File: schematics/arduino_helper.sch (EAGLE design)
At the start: 8 parts, among them Q1 L78M05CDT

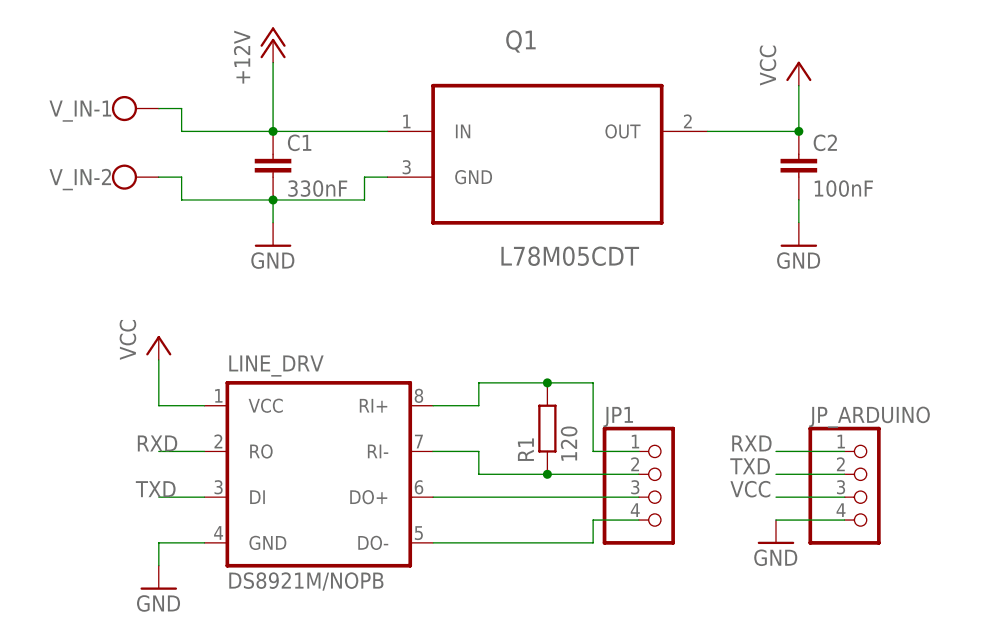
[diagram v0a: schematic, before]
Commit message: Extra caps, wider supply traces for the Arduino helper PCB.
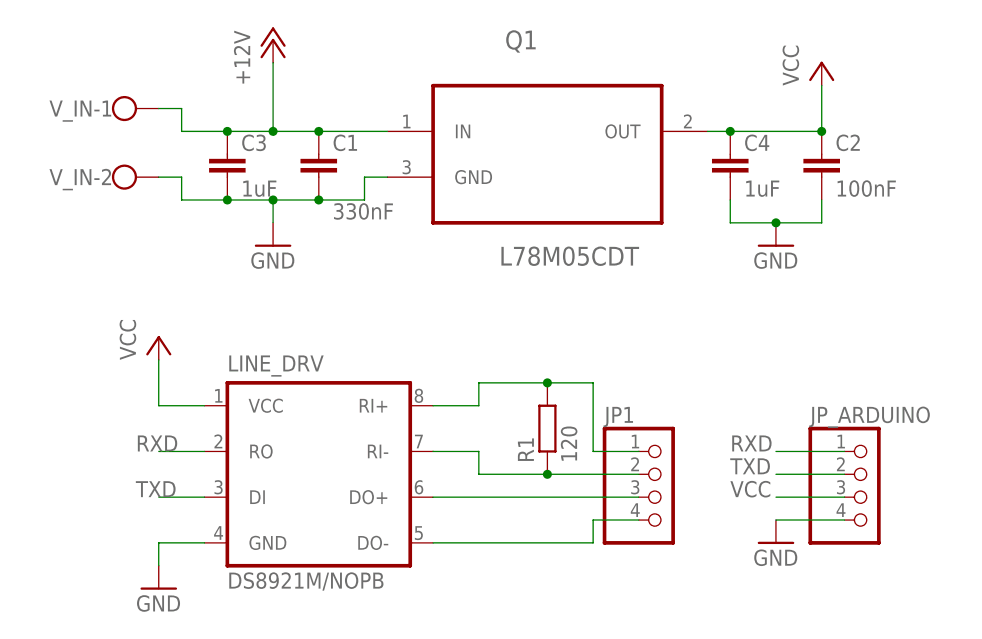
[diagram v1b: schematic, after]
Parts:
- added C3, C4: 1uF, rcl:C-EUC0805
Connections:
- net +12V: now also C3.1
- net GND: now also C3.2, C4.2
- net VCC: now also C4.1
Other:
- moved on the sheet: C1, C2
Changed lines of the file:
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@@
 <part name="GND4" library="supply1" deviceset="GND" device=""/>
 <part name="P+3" library="supply1" deviceset="+12V" device=""/>
+<part name="C3" library="rcl" deviceset="C-EU" device="C0805" value="1uF"/>
+<part name="C4" library="rcl" deviceset="C-EU" device="C0805" value="1uF"/>
 </parts>
 <sheets>
@@
 <instance part="V_IN" gate="-2" x="7.62" y="25.4"/>
 <instance part="JP1" gate="A" x="68.58" y="-10.16"/>
-<instance part="C1" gate="G$1" x="25.4" y="27.94"/>
-<instance part="C2" gate="G$1" x="83.82" y="27.94"/>
-<instance part="GND1" gate="1" x="83.82" y="17.78"/>
-<instance part="P+1" gate="VCC" x="83.82" y="38.1"/>
+<instance part="C1" gate="G$1" x="30.48" y="27.94" smashed="yes">
+<attribute name="NAME" x="32.004" y="28.321" size="1.778" layer="95"/>
+<attribute name="VALUE" x="32.004" y="20.701" size="1.778" layer="96"/>
+</instance>
+<instance part="C2" gate="G$1" x="86.36" y="27.94"/>
+<instance part="GND1" gate="1" x="81.28" y="17.78"/>
+<instance part="P+1" gate="VCC" x="86.36" y="38.1"/>
 <instance part="GND2" gate="1" x="25.4" y="17.78"/>
 <instance part="P+2" gate="VCC" x="12.7" y="7.62"/>
@@
 <instance part="GND4" gate="1" x="81.28" y="-15.24"/>
 <instance part="P+3" gate="1" x="25.4" y="40.64"/>
+<instance part="C3" gate="G$1" x="20.32" y="27.94"/>
+<instance part="C4" gate="G$1" x="76.2" y="27.94"/>
 </instances>
 <busses>
@@
 <segment>
 <pinref part="C2" gate="G$1" pin="2"/>
-<wire x1="83.82" y1="22.86" x2="83.82" y2="20.32" width="0.1524" layer="91"/>
 <pinref part="GND1" gate="1" pin="GND"/>
+<pinref part="C4" gate="G$1" pin="2"/>
+<wire x1="76.2" y1="22.86" x2="76.2" y2="20.32" width="0.1524" layer="91"/>
+<wire x1="76.2" y1="20.32" x2="81.28" y2="20.32" width="0.1524" layer="91"/>
+<wire x1="81.28" y1="20.32" x2="86.36" y2="20.32" width="0.1524" layer="91"/>
+<wire x1="86.36" y1="20.32" x2="86.36" y2="22.86" width="0.1524" layer="91"/>
+<junction x="81.28" y="20.32"/>
 </segment>
 <segment>
@@
 <wire x1="35.56" y1="25.4" x2="35.56" y2="22.86" width="0.1524" layer="91"/>
 <pinref part="C1" gate="G$1" pin="2"/>
-<wire x1="35.56" y1="22.86" x2="25.4" y2="22.86" width="0.1524" layer="91"/>
-<wire x1="25.4" y1="22.86" x2="15.24" y2="22.86" width="0.1524" layer="91"/>
+<wire x1="35.56" y1="22.86" x2="30.48" y2="22.86" width="0.1524" layer="91"/>
+<wire x1="30.48" y1="22.86" x2="25.4" y2="22.86" width="0.1524" layer="91"/>
+<wire x1="25.4" y1="22.86" x2="20.32" y2="22.86" width="0.1524" layer="91"/>
+<wire x1="20.32" y1="22.86" x2="15.24" y2="22.86" width="0.1524" layer="91"/>
 <wire x1="15.24" y1="22.86" x2="15.24" y2="25.4" width="0.1524" layer="91"/>
 <pinref part="V_IN" gate="-2" pin="KL"/>
 <wire x1="15.24" y1="25.4" x2="12.7" y2="25.4" width="0.1524" layer="91"/>
+<junction x="30.48" y="22.86"/>
+<pinref part="GND2" gate="1" pin="GND"/>
+<pinref part="C3" gate="G$1" pin="2"/>
+<junction x="20.32" y="22.86"/>
+<wire x1="25.4" y1="20.32" x2="25.4" y2="22.86" width="0.1524" layer="91"/>
 <junction x="25.4" y="22.86"/>
-<wire x1="25.4" y1="22.86" x2="25.4" y2="20.32" width="0.1524" layer="91"/>
-<pinref part="GND2" gate="1" pin="GND"/>
 </segment>
 <segment>
@@
 <pinref part="Q1" gate="A" pin="OUT"/>
 <pinref part="C2" gate="G$1" pin="1"/>
-<wire x1="73.66" y1="30.48" x2="83.82" y2="30.48" width="0.1524" layer="91"/>
-<wire x1="83.82" y1="30.48" x2="83.82" y2="35.56" width="0.1524" layer="91"/>
-<junction x="83.82" y="30.48"/>
+<wire x1="73.66" y1="30.48" x2="76.2" y2="30.48" width="0.1524" layer="91"/>
+<wire x1="76.2" y1="30.48" x2="86.36" y2="30.48" width="0.1524" layer="91"/>
+<wire x1="86.36" y1="30.48" x2="86.36" y2="35.56" width="0.1524" layer="91"/>
+<junction x="86.36" y="30.48"/>
 <pinref part="P+1" gate="VCC" pin="VCC"/>
+<pinref part="C4" gate="G$1" pin="1"/>
+<junction x="76.2" y="30.48"/>
 </segment>
 <segment>
@@
 <pinref part="Q1" gate="A" pin="IN"/>
 <pinref part="C1" gate="G$1" pin="1"/>
-<wire x1="38.1" y1="30.48" x2="25.4" y2="30.48" width="0.1524" layer="91"/>
-<wire x1="25.4" y1="30.48" x2="15.24" y2="30.48" width="0.1524" layer="91"/>
+<wire x1="38.1" y1="30.48" x2="30.48" y2="30.48" width="0.1524" layer="91"/>
+<wire x1="30.48" y1="30.48" x2="25.4" y2="30.48" width="0.1524" layer="91"/>
+<wire x1="25.4" y1="30.48" x2="20.32" y2="30.48" width="0.1524" layer="91"/>
+<wire x1="20.32" y1="30.48" x2="15.24" y2="30.48" width="0.1524" layer="91"/>
 <wire x1="15.24" y1="30.48" x2="15.24" y2="33.02" width="0.1524" layer="91"/>
 <pinref part="V_IN" gate="-1" pin="KL"/>
 <wire x1="15.24" y1="33.02" x2="12.7" y2="33.02" width="0.1524" layer="91"/>
+<junction x="30.48" y="30.48"/>
+<pinref part="P+3" gate="1" pin="+12V"/>
+<pinref part="C3" gate="G$1" pin="1"/>
+<junction x="20.32" y="30.48"/>
+<wire x1="25.4" y1="38.1" x2="25.4" y2="30.48" width="0.1524" layer="91"/>
 <junction x="25.4" y="30.48"/>
-<wire x1="25.4" y1="30.48" x2="25.4" y2="38.1" width="0.1524" layer="91"/>
-<pinref part="P+3" gate="1" pin="+12V"/>
 </segment>
 </net>

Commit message: Added names to unnamed signals.
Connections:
- net N$1 renamed RI-
- net N$2 renamed RI+
- net N$3 renamed DO-
- net N$4 renamed DO+
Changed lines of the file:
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@@
 </busses>
 <nets>
-<net name="N$1" class="0">
+<net name="RI-" class="0">
 <segment>
 <pinref part="LINE_DRV" gate="G$1" pin="RI-"/>
@@
 </segment>
 </net>
-<net name="N$2" class="0">
+<net name="RI+" class="0">
 <segment>
 <pinref part="LINE_DRV" gate="G$1" pin="RI+"/>
@@
 </segment>
 </net>
-<net name="N$3" class="0">
+<net name="DO-" class="0">
 <segment>
 <pinref part="LINE_DRV" gate="G$1" pin="DO-"/>
@@
 </segment>
 </net>
-<net name="N$4" class="0">
+<net name="DO+" class="0">
 <segment>
 <pinref part="LINE_DRV" gate="G$1" pin="DO+"/>
